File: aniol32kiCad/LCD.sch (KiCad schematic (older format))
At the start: 6 parts

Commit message: lots of changes
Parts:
- removed U?: 74LS32, symbol 74xx:74LS32
- removed U?: 74LS08, symbol 74xx:74LS08
- removed U?: 74LS14, symbol 74xx:74LS14
- added unit 4 of U1
- added U2: 74LS14, Package_DIP:DIP-14_W7.62mm_Socket, symbol 74xx:74LS14
- added U5: 74LS08, Package_DIP:DIP-14_W7.62mm_Socket, symbol 74xx:74LS08
- LCD_CONN1: renamed from J?; footprint (none) -> Connector_PinHeader_2.54mm:PinHeader_1x16_P2.54mm_Vertical
- RV1: renamed from RV?; footprint (none) -> Potentiometer_THT:Potentiometer_TT_P0915N
- U1: renamed from U?; footprint (none) -> Package_DIP:DIP-14_W7.62mm_Socket
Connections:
- net LCDE: now also U2.4
- net RD: now also U5.12
- net WR: now also U5.13
- net at U1.8: now also U1.12
- new net: U1.11, U2.3
- new net: U1.13, U5.11
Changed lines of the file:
@@
 $Descr A4 11693 8268
 encoding utf-8
-Sheet 2 5
+Sheet 3 3
 Title ""
 Date ""
@@
 $EndDescr
 $Comp
-L 74xx:74LS32 U?
-U 2 1 61ADA71C
-P 2450 1600
-F 0 "U?" H 2450 1925 50  0000 C CNN
-F 1 "74LS32" H 2450 1834 50  0000 C CNN
-F 2 "" H 2450 1600 50  0001 C CNN
-F 3 "http://www.ti.com/lit/gpn/sn74LS32" H 2450 1600 50  0001 C CNN
-	2    2450 1600
-	1    0    0    -1
-$EndComp
-$Comp
-L 74xx:74LS32 U?
+L 74xx:74LS32 U1
 U 3 1 61ADA722
 P 1850 1250
-F 0 "U?" H 1850 1575 50  0000 C CNN
+F 0 "U1" H 1850 1575 50  0000 C CNN
 F 1 "74LS32" H 1850 1484 50  0000 C CNN
-F 2 "" H 1850 1250 50  0001 C CNN
+F 2 "Package_DIP:DIP-14_W7.62mm_Socket" H 1850 1250 50  0001 C CNN
 F 3 "http://www.ti.com/lit/gpn/sn74LS32" H 1850 1250 50  0001 C CNN
 	3    1850 1250
@@
 Wire Wire Line
 	1300 1350 1550 1350
-$Comp
-L 74xx:74LS08 U?
-U 2 1 61ADA72D
-P 1850 1900
-F 0 "U?" H 1850 2225 50  0000 C CNN
-F 1 "74LS08" H 1850 2134 50  0000 C CNN
-F 2 "" H 1850 1900 50  0001 C CNN
-F 3 "http://www.ti.com/lit/gpn/sn74LS08" H 1850 1900 50  0001 C CNN
-	2    1850 1900
-	1    0    0    -1
-$EndComp
 Wire Wire Line
 	2150 1900 2150 1700
@@
 Wire Wire Line
 	1300 2000 1550 2000
-$Comp
-L 74xx:74LS14 U?
-U 1 1 61ADA738
-P 3050 1600
-F 0 "U?" H 3050 1917 50  0000 C CNN
-F 1 "74LS14" H 3050 1826 50  0000 C CNN
-F 2 "" H 3050 1600 50  0001 C CNN
-F 3 "http://www.ti.com/lit/gpn/sn74LS14" H 3050 1600 50  0001 C CNN
-	1    3050 1600
-	1    0    0    -1
-$EndComp
 Text GLabel 3350 1600 2    50   Input ~ 0
 LCDE
 $Comp
-L Connector:Conn_01x16_Male J?
+L Connector:Conn_01x16_Male LCD_CONN1
 U 1 1 61ADAD92
 P 2150 2950
-F 0 "J?" V 1985 2878 50  0000 C CNN
+F 0 "LCD_CONN1" V 1985 2878 50  0000 C CNN
 F 1 "Conn_01x16_Male" V 2076 2878 50  0000 C CNN
-F 2 "" H 2150 2950 50  0001 C CNN
+F 2 "Connector_PinHeader_2.54mm:PinHeader_1x16_P2.54mm_Vertical" H 2150 2950 50  0001 C CNN
 F 3 "~" H 2150 2950 50  0001 C CNN
 	1    2150 2950
@@
 LCDE
 $Comp
-L power:GND #PWR?
+L power:GND #PWR039
 U 1 1 61ADEFAF
 P 2850 3800
-F 0 "#PWR?" H 2850 3550 50  0001 C CNN
+F 0 "#PWR039" H 2850 3550 50  0001 C CNN
 F 1 "GND" H 2855 3627 50  0000 C CNN
 F 2 "" H 2850 3800 50  0001 C CNN
@@
 $EndComp
 $Comp
-L power:GND #PWR?
+L power:GND #PWR038
 U 1 1 61ADF325
 P 1350 3800
-F 0 "#PWR?" H 1350 3550 50  0001 C CNN
+F 0 "#PWR038" H 1350 3550 50  0001 C CNN
 F 1 "GND" H 1355 3627 50  0000 C CNN
 F 2 "" H 1350 3800 50  0001 C CNN
@@
 $EndComp
 $Comp
-L power:+5V #PWR?
+L power:+5V #PWR037
 U 1 1 61ADF9CB
 P 1050 2950
-F 0 "#PWR?" H 1050 2800 50  0001 C CNN
+F 0 "#PWR037" H 1050 2800 50  0001 C CNN
 F 1 "+5V" H 1065 3123 50  0000 C CNN
 F 2 "" H 1050 2950 50  0001 C CNN
@@
 D7
 $Comp
-L Device:R_POT_TRIM RV?
+L Device:R_POT_TRIM RV1
 U 1 1 61AE3A01
 P 3000 2350
-F 0 "RV?" H 2930 2396 50  0000 R CNN
+F 0 "RV1" H 2930 2396 50  0000 R CNN
 F 1 "R_POT_TRIM" H 2930 2305 50  0000 R CNN
-F 2 "" H 3000 2350 50  0001 C CNN
+F 2 "Potentiometer_THT:Potentiometer_TT_P0915N" H 3000 2350 50  0001 C CNN
 F 3 "~" H 3000 2350 50  0001 C CNN
 	1    3000 2350
@@
 $EndComp
 $Comp
-L power:GND #PWR?
+L power:GND #PWR041
 U 1 1 61AE450B
 P 3000 2500
-F 0 "#PWR?" H 3000 2250 50  0001 C CNN
+F 0 "#PWR041" H 3000 2250 50  0001 C CNN
 F 1 "GND" H 3005 2327 50  0000 C CNN
 F 2 "" H 3000 2500 50  0001 C CNN
@@
 $EndComp
 $Comp
-L power:+5V #PWR?
+L power:+5V #PWR040
 U 1 1 61AE48A7
 P 3000 2200
-F 0 "#PWR?" H 3000 2050 50  0001 C CNN
+F 0 "#PWR040" H 3000 2050 50  0001 C CNN
 F 1 "+5V" H 3015 2373 50  0000 C CNN
 F 2 "" H 3000 2200 50  0001 C CNN
@@
 Text GLabel 2450 3150 3    50   Input ~ 0
 A1
+$Comp
+L 74xx:74LS32 U1
+U 4 1 61CF0CC8
+P 2450 1600
+F 0 "U1" H 2450 1925 50  0000 C CNN
+F 1 "74LS32" H 2450 1834 50  0000 C CNN
+F 2 "Package_DIP:DIP-14_W7.62mm_Socket" H 2450 1600 50  0001 C CNN
+F 3 "http://www.ti.com/lit/gpn/sn74LS32" H 2450 1600 50  0001 C CNN
+	4    2450 1600
+	1    0    0    -1
+$EndComp
+$Comp
+L 74xx:74LS14 U2
+U 2 1 61CF53F8
+P 3050 1600
+F 0 "U2" H 3050 1917 50  0000 C CNN
+F 1 "74LS14" H 3050 1826 50  0000 C CNN
+F 2 "Package_DIP:DIP-14_W7.62mm_Socket" H 3050 1600 50  0001 C CNN
+F 3 "http://www.ti.com/lit/gpn/sn74LS14" H 3050 1600 50  0001 C CNN
+	2    3050 1600
+	1    0    0    -1
+$EndComp
+$Comp
+L 74xx:74LS08 U5
+U 4 1 61D0B6D4
+P 1850 1900
+F 0 "U5" H 1850 2225 50  0000 C CNN
+F 1 "74LS08" H 1850 2134 50  0000 C CNN
+F 2 "Package_DIP:DIP-14_W7.62mm_Socket" H 1850 1900 50  0001 C CNN
+F 3 "http://www.ti.com/lit/gpn/sn74LS08" H 1850 1900 50  0001 C CNN
+	4    1850 1900
+	1    0    0    -1
+$EndComp
 $EndSCHEMATC

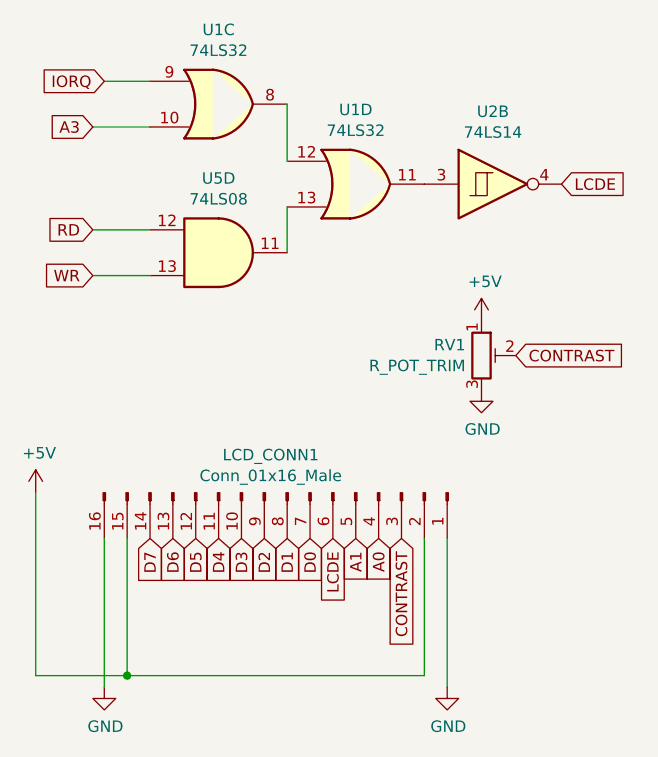
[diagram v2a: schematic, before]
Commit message: Doc changes
Removed a '32 from A32
Documented the VGA connector
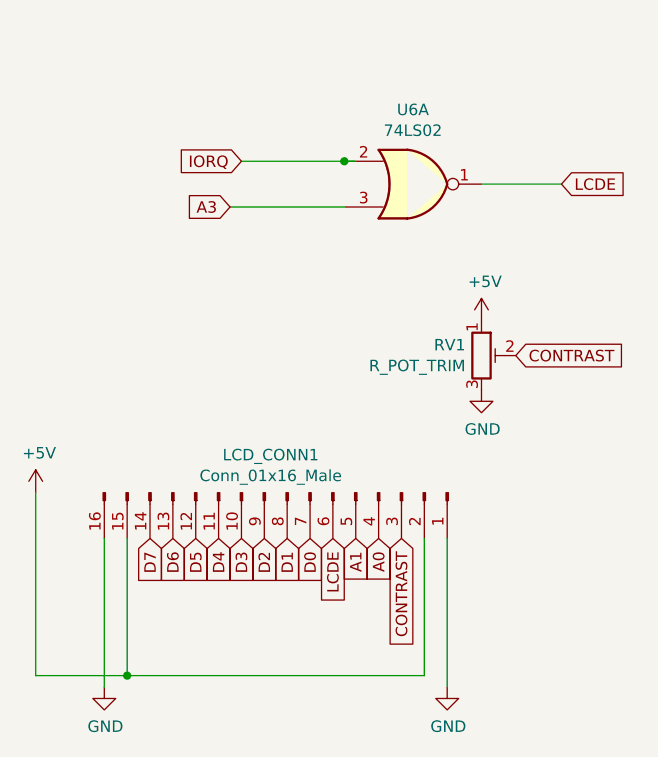
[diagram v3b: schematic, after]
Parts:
- removed U1: 74LS32, Package_DIP:DIP-14_W7.62mm_Socket, symbol 74xx:74LS32
- removed U2: 74LS14, Package_DIP:DIP-14_W7.62mm_Socket, symbol 74xx:74LS14
- removed U5: 74LS08, Package_DIP:DIP-14_W7.62mm_Socket, symbol 74xx:74LS08
- added U6: 74LS02, Package_DIP:DIP-14_W7.62mm_Socket, symbol 74xx:74LS02
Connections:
- net labels removed: RD, WR
- wire segments 13 -> 11
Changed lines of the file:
@@
 Comment4 ""
 $EndDescr
-$Comp
-L 74xx:74LS32 U1
-U 3 1 61ADA722
-P 1850 1250
-F 0 "U1" H 1850 1575 50  0000 C CNN
-F 1 "74LS32" H 1850 1484 50  0000 C CNN
-F 2 "Package_DIP:DIP-14_W7.62mm_Socket" H 1850 1250 50  0001 C CNN
-F 3 "http://www.ti.com/lit/gpn/sn74LS32" H 1850 1250 50  0001 C CNN
-	3    1850 1250
-	1    0    0    -1
-$EndComp
-Wire Wire Line
-	2150 1250 2150 1500
-Text GLabel 1350 1150 0    50   Input ~ 0
+Text GLabel 1950 1500 0    50   Input ~ 0
 IORQ
-Wire Wire Line
-	1350 1150 1550 1150
-Text GLabel 1300 1350 0    50   Input ~ 0
+Text GLabel 1900 1700 0    50   Input ~ 0
 A3
-Wire Wire Line
-	1300 1350 1550 1350
-Wire Wire Line
-	2150 1900 2150 1700
-Text GLabel 1300 1800 0    50   Input ~ 0
-RD
-Wire Wire Line
-	1300 1800 1550 1800
-Text GLabel 1300 2000 0    50   Input ~ 0
-WR
-Wire Wire Line
-	1300 2000 1550 2000
 Text GLabel 3350 1600 2    50   Input ~ 0
 LCDE
@@
 A1
 $Comp
-L 74xx:74LS32 U1
-U 4 1 61CF0CC8
-P 2450 1600
-F 0 "U1" H 2450 1925 50  0000 C CNN
-F 1 "74LS32" H 2450 1834 50  0000 C CNN
-F 2 "Package_DIP:DIP-14_W7.62mm_Socket" H 2450 1600 50  0001 C CNN
-F 3 "http://www.ti.com/lit/gpn/sn74LS32" H 2450 1600 50  0001 C CNN
-	4    2450 1600
+L 74xx:74LS02 U6
+U 1 1 621E8D35
+P 2700 1600
+F 0 "U6" H 2700 1925 50  0000 C CNN
+F 1 "74LS02" H 2700 1834 50  0000 C CNN
+F 2 "Package_DIP:DIP-14_W7.62mm_Socket" H 2700 1600 50  0001 C CNN
+F 3 "http://www.ti.com/lit/gpn/sn74ls02" H 2700 1600 50  0001 C CNN
+	1    2700 1600
 	1    0    0    -1
 $EndComp
-$Comp
-L 74xx:74LS14 U2
-U 2 1 61CF53F8
-P 3050 1600
-F 0 "U2" H 3050 1917 50  0000 C CNN
-F 1 "74LS14" H 3050 1826 50  0000 C CNN
-F 2 "Package_DIP:DIP-14_W7.62mm_Socket" H 3050 1600 50  0001 C CNN
-F 3 "http://www.ti.com/lit/gpn/sn74LS14" H 3050 1600 50  0001 C CNN
-	2    3050 1600
-	1    0    0    -1
-$EndComp
-$Comp
-L 74xx:74LS08 U5
-U 4 1 61D0B6D4
-P 1850 1900
-F 0 "U5" H 1850 2225 50  0000 C CNN
-F 1 "74LS08" H 1850 2134 50  0000 C CNN
-F 2 "Package_DIP:DIP-14_W7.62mm_Socket" H 1850 1900 50  0001 C CNN
-F 3 "http://www.ti.com/lit/gpn/sn74LS08" H 1850 1900 50  0001 C CNN
-	4    1850 1900
-	1    0    0    -1
-$EndComp
+Wire Wire Line
+	1950 1500 2400 1500
+Connection ~ 2400 1500
+Wire Wire Line
+	2400 1500 2450 1500
+Wire Wire Line
+	1900 1700 2400 1700
+Wire Wire Line
+	3350 1600 3000 1600
 $EndSCHEMATC
